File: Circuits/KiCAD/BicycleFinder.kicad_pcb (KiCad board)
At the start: 2 copper layers, 0 parts

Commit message: Made an example layout.
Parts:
- added BT1: 3V, CR2032H, F.Cu at (37.5, 24.1)
- added C1: 1F, CP_22x41mm, F.Cu at (38.7, 47.6)
- added P1: CONN_14, SIL-14, F.Cu at (68.6, 48.9)
- added P2: CONN_14, SIL-14, F.Cu at (68.6, 15.2)
- added SW1: SW_PUSH, SW_PUSH-12mm, F.Cu at (21.0, 35.6)
- added U1: LITE_LITE, LITE, B.Cu at (59.7, 39.4)
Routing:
- net GND: track 0.00 -> 88.1 mm
- net VCC: track 0.00 -> 39.0 mm
- net /DI1: track 0.00 -> 35.7 mm, vias 0 -> 1
- net /SCL: track 0.00 -> 33.9 mm, vias 0 -> 1
- net /RXD: track 0.00 -> 27.8 mm, vias 0 -> 1
- net /M1: track 0.00 -> 22.2 mm, vias 0 -> 1
- net /DO4: track 0.00 -> 19.0 mm, vias 0 -> 1
- net /DI2: track 0.00 -> 17.6 mm, vias 0 -> 1
- net /PWM4: track 0.00 -> 15.9 mm, vias 0 -> 1
- net /DI3: track 0.00 -> 14.0 mm, vias 0 -> 1
- net /TX: track 0.00 -> 10.7 mm, vias 0 -> 1
- net /PWM2: track 0.00 -> 10.7 mm, vias 0 -> 1
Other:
- board outline added: 74.9 x 46.4 mm

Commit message: CS75サイズ検討中。
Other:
- board size 74.9 x 46.4 mm -> 3.3 x 4.3 mm

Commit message: Trying layout on TAKACHI PS-85.
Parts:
- added PS-85: VAL**, PS-85, F.Cu at (47.0, 32.4)
- added R1: 1k, R4, F.Cu at (38.7, 28.6)
- moved U1 43.8 mm to (15.9, 38.1)
- moved C1 38.4 mm to (73.7, 31.8)
- moved SW1 29.9 mm to (50.8, 34.3)
- moved P1 19.4 mm to (49.5, 45.1)
- moved BT1 16.8 mm to (24.1, 34.3), turned to 75 degrees
- moved P2 15.1 mm to (54.0, 19.1)
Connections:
- BT1 pad 1: VCC -> N-000002
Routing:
- net (no net): track 0.00 -> 251.3 mm, vias 0 -> 8
- net GND: track 88.1 -> 0.00 mm
- net VCC: track 39.0 -> 0.00 mm
- net /RST: track 0.00 -> 39.0 mm
- net /DI1: track 35.7 -> 0.00 mm, vias 1 -> 0
- net /SCL: track 33.9 -> 0.00 mm, vias 1 -> 0
- net /RXD: track 27.8 -> 0.00 mm, vias 1 -> 0
- net /M1: track 22.2 -> 0.00 mm, vias 1 -> 0
- net /DO4: track 19.0 -> 0.00 mm, vias 1 -> 0
- net /DI2: track 17.6 -> 0.00 mm, vias 1 -> 0
- net /AI1: track 0.00 -> 17.6 mm, vias 0 -> 1
- net /PWM4: track 15.9 -> 0.00 mm, vias 1 -> 0
- net /DI3: track 14.0 -> 0.00 mm, vias 1 -> 0
- net /TX: track 10.7 -> 0.00 mm, vias 1 -> 0
- net /PWM2: track 10.7 -> 12.7 mm, vias 1 -> 0

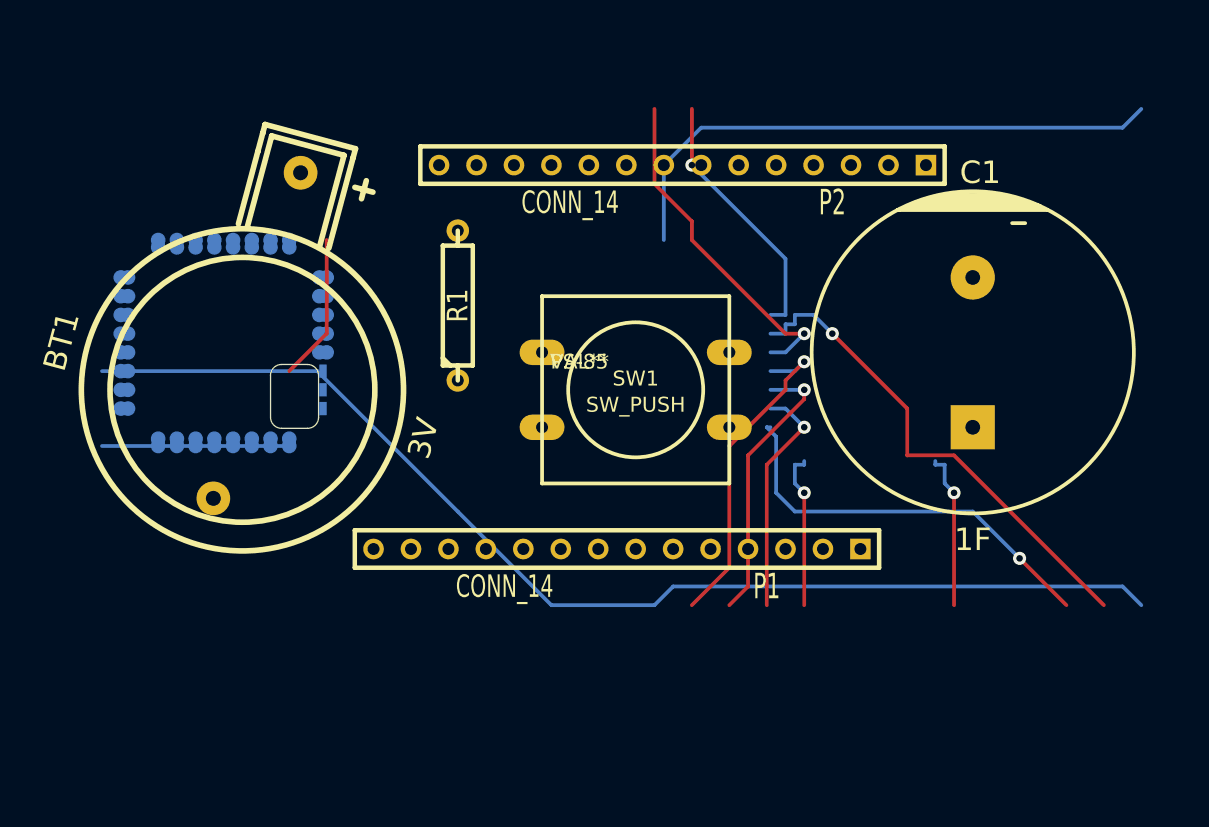
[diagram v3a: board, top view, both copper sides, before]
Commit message: Removed old route.
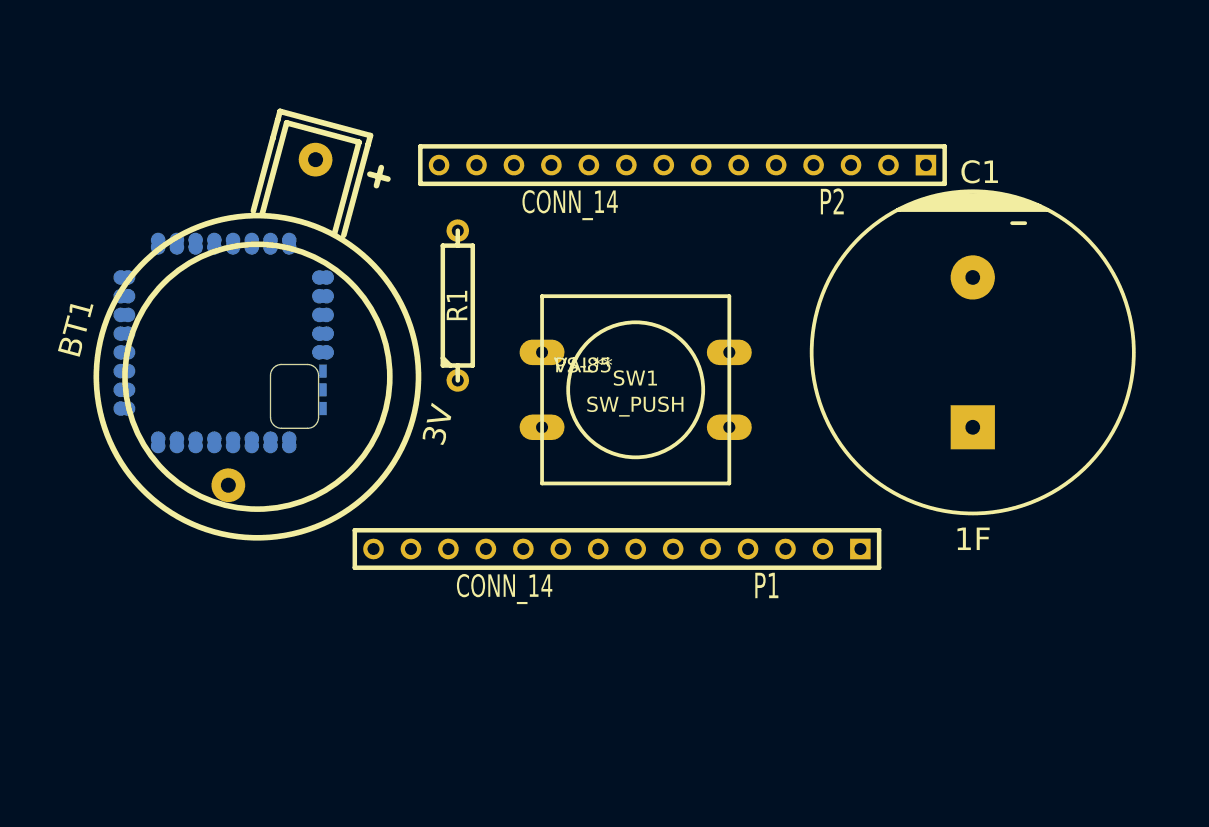
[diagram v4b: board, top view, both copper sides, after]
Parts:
- moved BT1 1.35 mm to (25.1, 33.4)
- moved PS-85 0.36 mm to (47.2, 32.6)
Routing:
- net (no net): track 251.3 -> 0.00 mm, vias 8 -> 0
- net /RST: track 39.0 -> 0.00 mm
- net /AI1: track 17.6 -> 0.00 mm, vias 1 -> 0
- net /PWM2: track 12.7 -> 0.00 mm

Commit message: Added monitor LED.
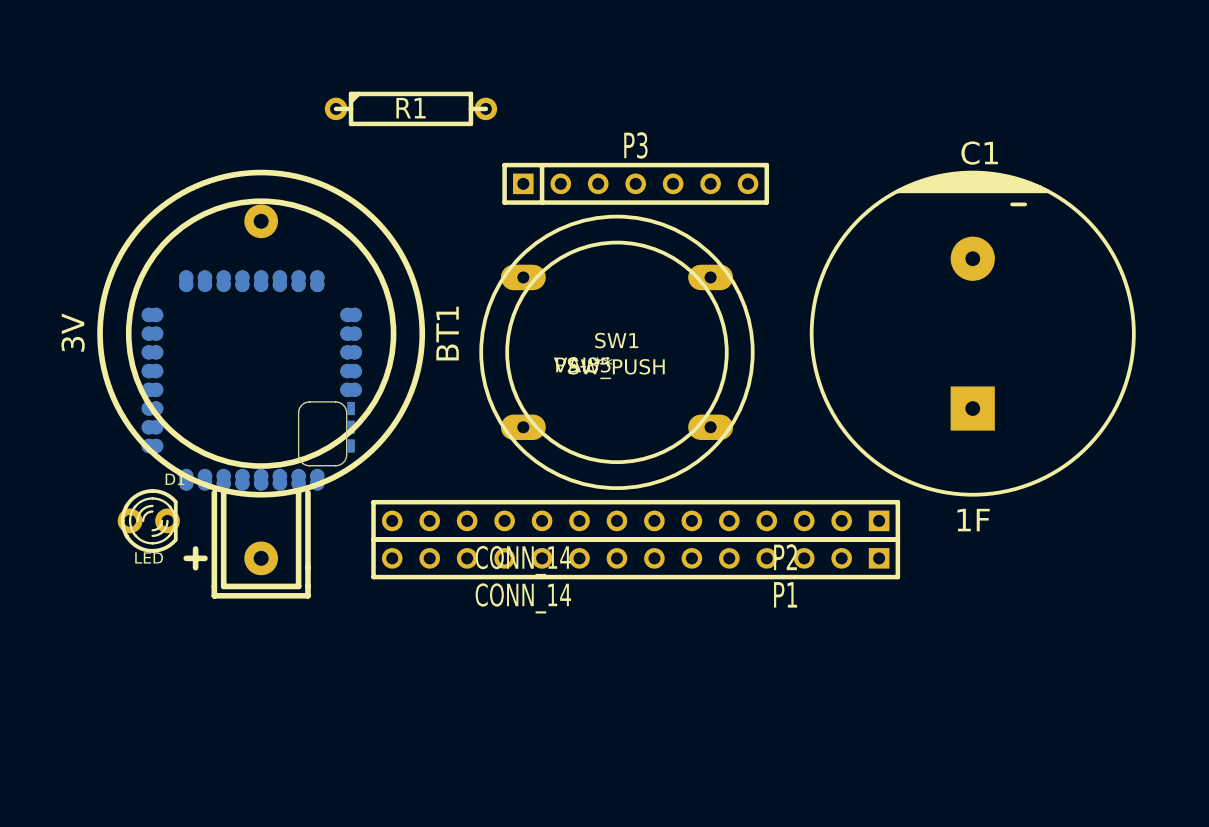
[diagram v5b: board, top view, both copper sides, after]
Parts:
- added D1: LED, LED-3MM, F.Cu at (17.8, 43.2)
- added P3: CONN_7, SIL-7, F.Cu at (50.8, 20.3)
- SW1: footprint SW_PUSH-12mm -> SW_PUSH-18mm
- moved P2 24.3 mm to (50.8, 43.2)
- moved R1 13.7 mm to (35.6, 15.2), turned to 0 degrees
- moved U1 3.18 mm to (17.8, 40.6)
- moved BT1 2.93 mm to (25.4, 30.5), turned to 270 degrees
- moved SW1 2.84 mm to (49.5, 31.8)
- moved P1 1.42 mm to (50.8, 45.7)
- moved C1 1.27 mm to (73.7, 30.5)
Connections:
- BT1 pad 1: N-000002 -> N-000001
- C1 pad 1: VCC -> /Vcc
- P1 pad 10: /TX -> /RXD
- P1 pad 3: /RXD -> /TXD
- P2 pad 1: VCC -> /Vcc
- R1 pad 1: VCC -> N-000001
- R1 pad 2: N-000002 -> /Vcc
- U1 pad 5: VCC -> /Vcc
- U1 pad 8: /TX -> /RXD
- U1 pad 9: /RXD -> /TXD
